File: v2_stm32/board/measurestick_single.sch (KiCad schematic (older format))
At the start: 5 parts, among them IC1 LM393, J9 USB_A

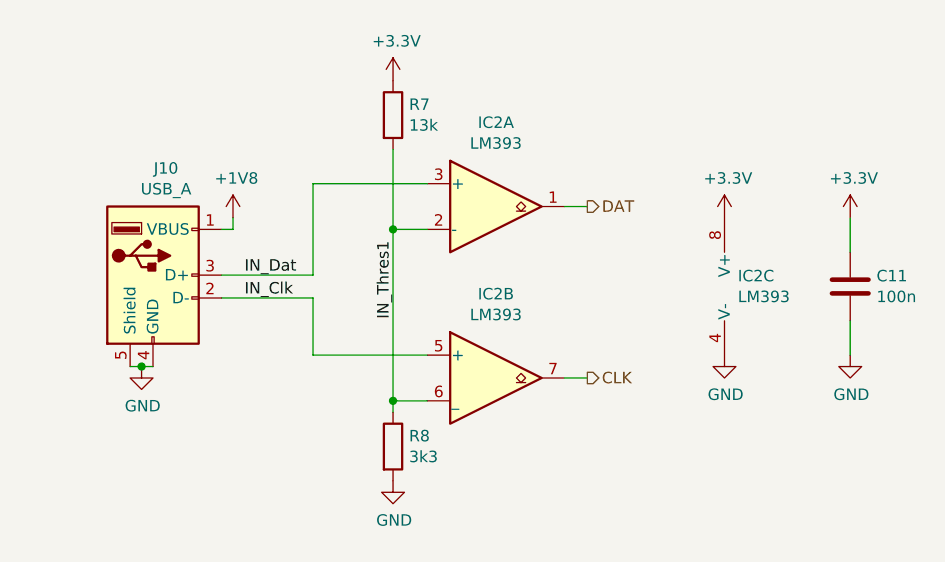
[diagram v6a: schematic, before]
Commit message: Changed MS DAT/CLK pins. Routed measuring stick input
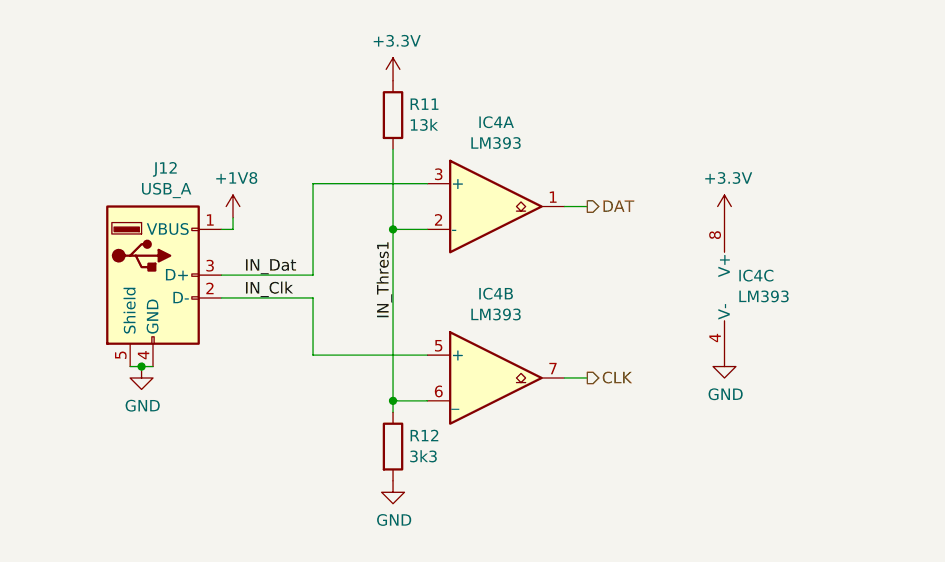
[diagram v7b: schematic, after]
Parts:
- removed C10: 100n, Capacitor_SMD:C_0603_1608Metric, symbol Device:C
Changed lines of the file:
@@
 $Descr A4 11693 8268
 encoding utf-8
-Sheet 3 7
+Sheet 5 7
 Title ""
 Date ""
@@
 AR Path="/60265FC9/60261634" Ref="IC3"  Part="2"
 AR Path="/6026601C/60261634" Ref="IC4"  Part="2"
-F 0 "IC2" H 3850 3817 50  0000 C CNN
+F 0 "IC4" H 3850 3817 50  0000 C CNN
 F 1 "LM393" H 3850 3726 50  0000 C CNN
 F 2 "Package_SO:SOIC-8_3.9x4.9mm_P1.27mm" H 3850 3450 50  0001 C CNN
@@
 AR Path="/60265FC9/6026163B" Ref="IC3"  Part="1"
 AR Path="/6026601C/6026163B" Ref="IC4"  Part="1"
-F 0 "IC2" H 3850 3067 50  0000 C CNN
+F 0 "IC4" H 3850 3067 50  0000 C CNN
 F 1 "LM393" H 3850 2976 50  0000 C CNN
 F 2 "Package_SO:SOIC-8_3.9x4.9mm_P1.27mm" H 3850 2700 50  0001 C CNN
@@
 AR Path="/60265FC9/60261641" Ref="IC3"  Part="3"
 AR Path="/6026601C/60261641" Ref="IC4"  Part="3"
-F 0 "IC2" H 4908 3096 50  0000 L CNN
+F 0 "IC4" H 4908 3096 50  0000 L CNN
 F 1 "LM393" H 4908 3005 50  0000 L CNN
 F 2 "Package_SO:SOIC-8_3.9x4.9mm_P1.27mm" H 4950 3050 50  0001 C CNN
@@
 AR Path="/6026601C/60261659" Ref="J12"  Part="1"
 AR Path="/60261659" Ref="J?"  Part="1"
-F 0 "J10" H 2407 3467 50  0000 C CNN
+F 0 "J12" H 2407 3467 50  0000 C CNN
 F 1 "USB_A" H 2407 3376 50  0000 C CNN
 F 2 "Lathecontrol_STM32:USB_A_Upright_C26235" H 2500 2950 50  0001 C CNN
@@
 AR Path="/60265FC9/6026167C" Ref="R9"  Part="1"
 AR Path="/6026601C/6026167C" Ref="R11"  Part="1"
-F 0 "R7" H 3470 2346 50  0000 L CNN
+F 0 "R11" H 3470 2346 50  0000 L CNN
 F 1 "13k" H 3470 2255 50  0000 L CNN
 F 2 "Resistor_SMD:R_0603_1608Metric" V 3330 2300 50  0001 C CNN
@@
 AR Path="/60265FC9/60261683" Ref="R10"  Part="1"
 AR Path="/6026601C/60261683" Ref="R12"  Part="1"
-F 0 "R8" H 3470 3796 50  0000 L CNN
+F 0 "R12" H 3470 3796 50  0000 L CNN
 F 1 "3k3" H 3470 3705 50  0000 L CNN
 F 2 "Resistor_SMD:R_0603_1608Metric" V 3330 3750 50  0001 C CNN
@@
 $EndComp
 $Comp
-L Device:C C?
-U 1 1 6026169F
-P 5400 3050
-AR Path="/6025D9E2/6026169F" Ref="C?"  Part="1"
-AR Path="/6025D9E2/6025E7C0/6026169F" Ref="C?"  Part="1"
-AR Path="/6025D9E2/60265A76/6026169F" Ref="C?"  Part="1"
-AR Path="/6025D9E2/60265B58/6026169F" Ref="C?"  Part="1"
-AR Path="/6025D9E2/60265BB4/6026169F" Ref="C?"  Part="1"
-AR Path="/6025D9E2/60265C25/6026169F" Ref="C?"  Part="1"
-AR Path="/60265C89/6026169F" Ref="C10"  Part="1"
-AR Path="/60265F6D/6026169F" Ref="C11"  Part="1"
-AR Path="/60265FC9/6026169F" Ref="C12"  Part="1"
-AR Path="/6026601C/6026169F" Ref="C13"  Part="1"
-F 0 "C11" H 5515 3096 50  0000 L CNN
-F 1 "100n" H 5515 3005 50  0000 L CNN
-F 2 "Capacitor_SMD:C_0603_1608Metric" H 5438 2900 50  0001 C CNN
-F 3 "https://datasheet.lcsc.com/szlcsc/YAGEO-CC0603KRX7R9BB104_C14663.pdf" H 5400 3050 50  0001 C CNN
-F 4 "C14663" H 5400 3050 50  0001 C CNN "LCSC"
-	1    5400 3050
-	1    0    0    -1
-$EndComp
-$Comp
 L power:+3.3V #PWR?
-U 1 1 602616A5
-P 5400 2750
-AR Path="/6025D9E2/602616A5" Ref="#PWR?"  Part="1"
-AR Path="/6025D9E2/6025E7C0/602616A5" Ref="#PWR?"  Part="1"
-AR Path="/6025D9E2/60265A76/602616A5" Ref="#PWR?"  Part="1"
-AR Path="/6025D9E2/60265B58/602616A5" Ref="#PWR?"  Part="1"
-AR Path="/6025D9E2/60265BB4/602616A5" Ref="#PWR?"  Part="1"
-AR Path="/6025D9E2/60265C25/602616A5" Ref="#PWR?"  Part="1"
-AR Path="/60265C89/602616A5" Ref="#PWR043"  Part="1"
-AR Path="/60265F6D/602616A5" Ref="#PWR051"  Part="1"
-AR Path="/60265FC9/602616A5" Ref="#PWR059"  Part="1"
-AR Path="/6026601C/602616A5" Ref="#PWR067"  Part="1"
-F 0 "#PWR067" H 5400 2600 50  0001 C CNN
-F 1 "+3.3V" H 5415 2923 50  0000 C CNN
-F 2 "" H 5400 2750 50  0001 C CNN
-F 3 "" H 5400 2750 50  0001 C CNN
-	1    5400 2750
-	1    0    0    -1
-$EndComp
-$Comp
-L power:GND #PWR?
-U 1 1 602616AB
-P 5400 3350
-AR Path="/602616AB" Ref="#PWR?"  Part="1"
-AR Path="/6025D9E2/602616AB" Ref="#PWR?"  Part="1"
-AR Path="/6025D9E2/6025E7C0/602616AB" Ref="#PWR?"  Part="1"
-AR Path="/6025D9E2/60265A76/602616AB" Ref="#PWR?"  Part="1"
-AR Path="/6025D9E2/60265B58/602616AB" Ref="#PWR?"  Part="1"
-AR Path="/6025D9E2/60265BB4/602616AB" Ref="#PWR?"  Part="1"
-AR Path="/6025D9E2/60265C25/602616AB" Ref="#PWR?"  Part="1"
-AR Path="/60265C89/602616AB" Ref="#PWR044"  Part="1"
-AR Path="/60265F6D/602616AB" Ref="#PWR052"  Part="1"
-AR Path="/60265FC9/602616AB" Ref="#PWR060"  Part="1"
-AR Path="/6026601C/602616AB" Ref="#PWR068"  Part="1"
-F 0 "#PWR068" H 5400 3100 50  0001 C CNN
-F 1 "GND" H 5405 3177 50  0000 C CNN
-F 2 "" H 5400 3350 50  0001 C CNN
-F 3 "" H 5400 3350 50  0001 C CNN
-	1    5400 3350
-	1    0    0    -1
-$EndComp
-Wire Wire Line
-	5400 3200 5400 3350
-Wire Wire Line
-	5400 2750 5400 2900
-$Comp
-L power:+3.3V #PWR?

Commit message: More routing
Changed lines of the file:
@@
 $Descr A4 11693 8268
 encoding utf-8
-Sheet 5 7
+Sheet 2 7
 Title ""
 Date ""
@@
 AR Path="/60265FC9/60261634" Ref="IC3"  Part="2"
 AR Path="/6026601C/60261634" Ref="IC4"  Part="2"
-F 0 "IC4" H 3850 3817 50  0000 C CNN
+F 0 "IC1" H 3850 3817 50  0000 C CNN
 F 1 "LM393" H 3850 3726 50  0000 C CNN
 F 2 "Package_SO:SOIC-8_3.9x4.9mm_P1.27mm" H 3850 3450 50  0001 C CNN
@@
 AR Path="/60265FC9/6026163B" Ref="IC3"  Part="1"
 AR Path="/6026601C/6026163B" Ref="IC4"  Part="1"
-F 0 "IC4" H 3850 3067 50  0000 C CNN
+F 0 "IC1" H 3850 3067 50  0000 C CNN
 F 1 "LM393" H 3850 2976 50  0000 C CNN
 F 2 "Package_SO:SOIC-8_3.9x4.9mm_P1.27mm" H 3850 2700 50  0001 C CNN
@@
 AR Path="/60265FC9/60261641" Ref="IC3"  Part="3"
 AR Path="/6026601C/60261641" Ref="IC4"  Part="3"
-F 0 "IC4" H 4908 3096 50  0000 L CNN
+F 0 "IC1" H 4908 3096 50  0000 L CNN
 F 1 "LM393" H 4908 3005 50  0000 L CNN
 F 2 "Package_SO:SOIC-8_3.9x4.9mm_P1.27mm" H 4950 3050 50  0001 C CNN
@@
 AR Path="/60265FC9/60261649" Ref="#PWR058"  Part="1"
 AR Path="/6026601C/60261649" Ref="#PWR066"  Part="1"
-F 0 "#PWR066" H 4850 3100 50  0001 C CNN
+F 0 "#PWR042" H 4850 3100 50  0001 C CNN
 F 1 "GND" H 4855 3177 50  0000 C CNN
 F 2 "" H 4850 3350 50  0001 C CNN
@@
 AR Path="/6026601C/60261659" Ref="J12"  Part="1"
 AR Path="/60261659" Ref="J?"  Part="1"
-F 0 "J12" H 2407 3467 50  0000 C CNN
+F 0 "J9" H 2407 3467 50  0000 C CNN
 F 1 "USB_A" H 2407 3376 50  0000 C CNN
 F 2 "Lathecontrol_STM32:USB_A_Upright_C26235" H 2500 2950 50  0001 C CNN
@@
 AR Path="/60265FC9/60261663" Ref="#PWR053"  Part="1"
 AR Path="/6026601C/60261663" Ref="#PWR061"  Part="1"
-F 0 "#PWR061" H 2300 3150 50  0001 C CNN
+F 0 "#PWR037" H 2300 3150 50  0001 C CNN
 F 1 "GND" H 2305 3227 50  0000 C CNN
 F 2 "" H 2300 3400 50  0001 C CNN
@@
 AR Path="/60265FC9/6026166C" Ref="#PWR054"  Part="1"
 AR Path="/6026601C/6026166C" Ref="#PWR062"  Part="1"
-F 0 "#PWR062" H 2700 2600 50  0001 C CNN
+F 0 "#PWR038" H 2700 2600 50  0001 C CNN
 F 1 "+1V8" H 2715 2923 50  0000 C CNN
 F 2 "" H 2700 2750 50  0001 C CNN
@@
 AR Path="/60265FC9/6026167C" Ref="R9"  Part="1"
 AR Path="/6026601C/6026167C" Ref="R11"  Part="1"
-F 0 "R11" H 3470 2346 50  0000 L CNN
+F 0 "R5" H 3470 2346 50  0000 L CNN
 F 1 "13k" H 3470 2255 50  0000 L CNN
 F 2 "Resistor_SMD:R_0603_1608Metric" V 3330 2300 50  0001 C CNN
@@
 AR Path="/60265FC9/60261683" Ref="R10"  Part="1"
 AR Path="/6026601C/60261683" Ref="R12"  Part="1"
-F 0 "R12" H 3470 3796 50  0000 L CNN
+F 0 "R6" H 3470 3796 50  0000 L CNN
 F 1 "3k3" H 3470 3705 50  0000 L CNN
 F 2 "Resistor_SMD:R_0603_1608Metric" V 3330 3750 50  0001 C CNN
@@
 AR Path="/60265FC9/60261690" Ref="#PWR055"  Part="1"
 AR Path="/6026601C/60261690" Ref="#PWR063"  Part="1"
-F 0 "#PWR063" H 3400 2000 50  0001 C CNN
+F 0 "#PWR039" H 3400 2000 50  0001 C CNN
 F 1 "+3.3V" H 3415 2323 50  0000 C CNN
 F 2 "" H 3400 2150 50  0001 C CNN
@@
 AR Path="/60265FC9/60261696" Ref="#PWR056"  Part="1"
 AR Path="/6026601C/60261696" Ref="#PWR064"  Part="1"
-F 0 "#PWR064" H 3400 3650 50  0001 C CNN
+F 0 "#PWR040" H 3400 3650 50  0001 C CNN
 F 1 "GND" H 3405 3727 50  0000 C CNN
 F 2 "" H 3400 3900 50  0001 C CNN
@@
 AR Path="/60265FC9/60261675" Ref="#PWR057"  Part="1"
 AR Path="/6026601C/60261675" Ref="#PWR065"  Part="1"
-F 0 "#PWR065" H 4850 2600 50  0001 C CNN
+F 0 "#PWR041" H 4850 2600 50  0001 C CNN
 F 1 "+3.3V" H 4865 2923 50  0000 C CNN
 F 2 "" H 4850 2750 50  0001 C CNN
